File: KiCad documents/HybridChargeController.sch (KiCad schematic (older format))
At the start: 10 parts

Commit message: switched to transistors maybe need 10k
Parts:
- removed Q? (x3): 2N 7002, symbol Q_NMOS_GSD
- added Q? (x3): 2N3904, symbol Q_NPN_EBC
- added R?: 10k, symbol R
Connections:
- wire segments 28 -> 32
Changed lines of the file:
@@
-$EndComp
-$Comp
-L Q_NMOS_GSD Q?
-U 1 1 58D3AC23
-P 2950 4600
-F 0 "Q?" H 3250 4650 50  0000 R CNN
-F 1 "2N 7002" H 3450 4550 50  0000 R CNN
-F 2 "" H 3150 4700 50  0000 C CNN
-F 3 "" H 2950 4600 50  0000 C CNN
-	1    2950 4600
-	1    0    0    -1
 $EndComp
 $Comp
@@
 $EndComp
 $Comp
-L Q_NMOS_GSD Q?
-U 1 1 58D3CBFA
-P 2200 2050
-F 0 "Q?" H 2500 2100 50  0000 R CNN
-F 1 "2N 7002" H 2700 2000 50  0000 R CNN
-F 2 "" H 2400 2150 50  0000 C CNN
-F 3 "" H 2200 2050 50  0000 C CNN
-	1    2200 2050
-	1    0    0    -1
-$EndComp
-$Comp
 L Q_PMOS_GDS Q?
 U 1 1 58D3CC00
@@
 LA switch circuit \nLoad switch is closed, when SW_BAT is LOW
 $Comp
-L Q_NMOS_GSD Q?
-U 1 1 58D8C0D3
-P 1500 4750
-F 0 "Q?" H 1800 4800 50  0000 R CNN
-F 1 "2N 7002" H 2000 4700 50  0000 R CNN
-F 2 "" H 1700 4850 50  0000 C CNN
-F 3 "" H 1500 4750 50  0000 C CNN
-	1    1500 4750
-	1    0    0    -1
-$EndComp
-$Comp
 L R R?
 U 1 1 58D8C1D7
@@
 Wire Wire Line
 	1300 4750 1100 4750
+$Comp
+L Q_NPN_EBC Q?
+U 1 1 58D8E9F2
+P 1500 4750
+F 0 "Q?" H 1800 4800 50  0000 R CNN
+F 1 "2N3904" H 1950 4700 50  0000 R CNN
+F 2 "" H 1700 4850 50  0000 C CNN
+F 3 "" H 1500 4750 50  0000 C CNN
+	1    1500 4750
+	1    0    0    -1
+$EndComp
+$Comp
+L Q_NPN_EBC Q?
+U 1 1 58D8EBDE
+P 2950 4600
+F 0 "Q?" H 3250 4650 50  0000 R CNN
+F 1 "2N3904" H 3400 4550 50  0000 R CNN
+F 2 "" H 3150 4700 50  0000 C CNN
+F 3 "" H 2950 4600 50  0000 C CNN
+	1    2950 4600
+	1    0    0    -1
+$EndComp
+$Comp
+L Q_NPN_EBC Q?
+U 1 1 58D8EC57
+P 2200 2050
+F 0 "Q?" H 2500 2100 50  0000 R CNN
+F 1 "2N3904" H 2650 2000 50  0000 R CNN
+F 2 "" H 2400 2150 50  0000 C CNN
+F 3 "" H 2200 2050 50  0000 C CNN
+	1    2200 2050
+	1    0    0    -1
+$EndComp
+$Comp
+L R R?
+U 1 1 58D8EEFB
+P 3850 4400
+F 0 "R?" V 3930 4400 50  0000 C CNN
+F 1 "10k" V 3850 4400 50  0000 C CNN
+F 2 "" V 3780 4400 50  0000 C CNN
+F 3 "" H 3850 4400 50  0000 C CNN
+	1    3850 4400
+	1    0    0    -1
+$EndComp
+Wire Wire Line
+	3850 4250 3850 4000
+Connection ~ 3850 4000
+Wire Wire Line
+	3850 4550 3850 4900
+Wire Wire Line
+	3850 4900 3600 4900
+Wire Wire Line
+	3600 4900 3600 5200
+Connection ~ 3600 5200
 $EndSCHEMATC

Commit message: two mosfets on both power lines. working nicely
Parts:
- removed Q? (x2): IPD90P04P4_05, symbol Q_PMOS_GDS
- removed R?: 10k, symbol R
- added D?: D, symbol D
- added Q? (x5): IPD90P04P4_05, symbol Q_NMOS_GSD
- added Q?: 2N3904, symbol Q_NPN_EBC
- added R? (x3): 10k, symbol R
- added R?: 47k, symbol R
- added R?: 100k, symbol R
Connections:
- net labels added: COM+, LA+, LI+, LOAD+, SW_LA, SW_LI, SW_LOAD
- net labels removed: LA_12V, LA_GND, SW_BAT, VCC
- wire segments 32 -> 61
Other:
- note added: "????"
- note added: "LA switch circuit \nswitch is closed, when SW_LA is LOW"
- note added: "LI switch circuit \nswitch is open, when SW_LI is LOW"
- note added: "Load switch circuit \nswitch is open, when SW_LOAD is LOW"
- note removed: "LA switch circuit \nLoad switch is closed, when SW_BAT is LOW"
- moved on the sheet: Q?, R?

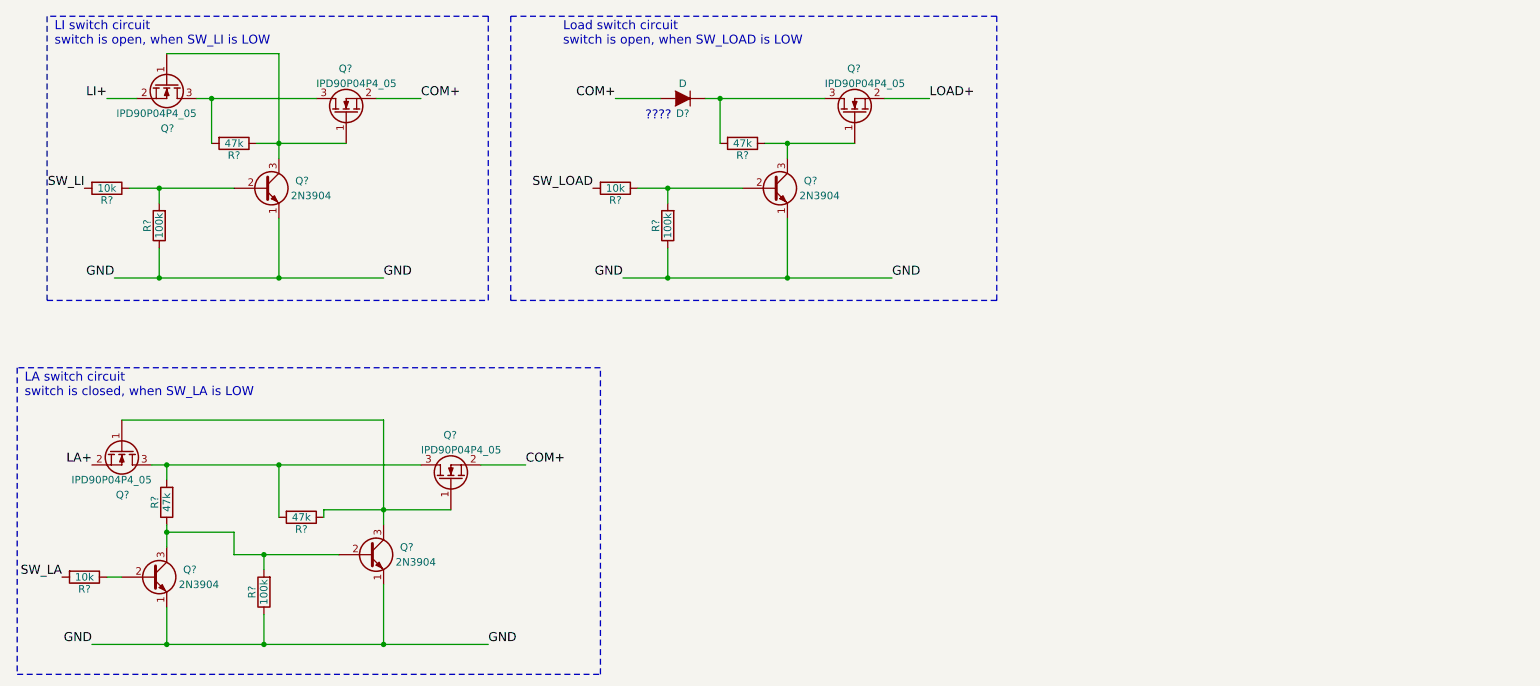
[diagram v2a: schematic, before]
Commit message: added arduinouno footprint
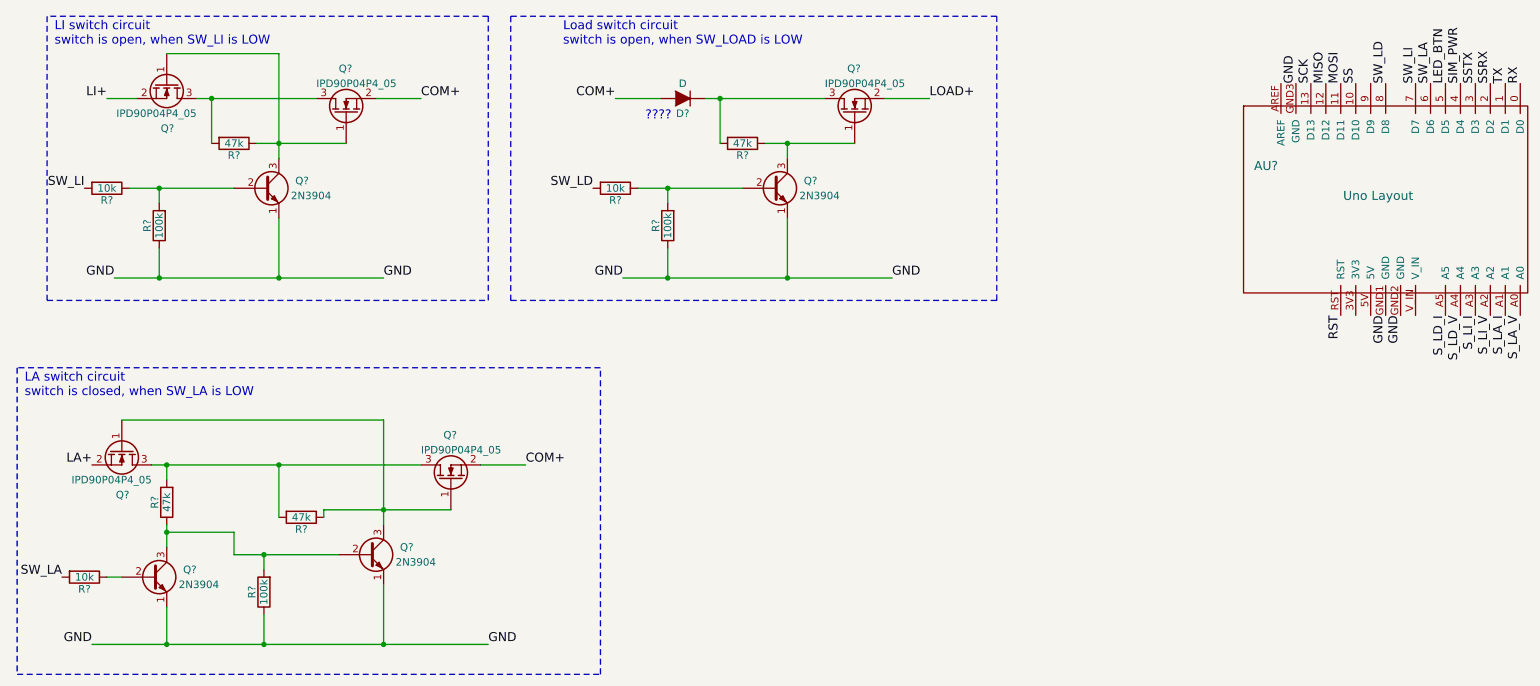
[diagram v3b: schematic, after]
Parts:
- added AU?: Uno Layout, symbol ArduinoUno
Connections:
- net GND: now also AU?.GND1 (GND), AU?.GND2 (GND), AU?.GND3 (GND)
- net SW_LA: now also AU?.6 (D6)
- net SW_LI: now also AU?.7 (D7)
- net SW_LOAD renamed SW_LD
- net SW_LD: now also AU?.8 (D8)
- new net LED_BTN: AU?.5 (D5)
- new net MISO: AU?.12 (D12)
- new net MOSI: AU?.11 (D11)
- new net RST: AU?.RST
- new net RX: AU?.0 (D0)
- new net SCK: AU?.13 (D13)
- new net SIM_PWR: AU?.4 (D4)
- new net SS: AU?.10 (D10)
- new net SSRX: AU?.2 (D2)
- new net SSTX: AU?.3 (D3)
- new net S_LA_I: AU?.A1
- new net S_LA_V: AU?.A0
- new net S_LD_I: AU?.A5
- new net S_LD_V: AU?.A4
- new net S_LI_I: AU?.A3
- new net S_LI_V: AU?.A2
- new net TX: AU?.1 (D1)
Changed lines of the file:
@@
 LIBS:contrib
 LIBS:valves
+LIBS:arduinouno
 LIBS:HybridChargeController-cache
 EELAYER 25 0
@@
 $EndComp
 Wire Wire Line
-	2600 3850 3000 3850
-Wire Wire Line
-	3000 3850 3450 3850
-Wire Wire Line
-	3000 3250 3000 3850
-Wire Wire Line
-	3000 3850 3000 3950
-Wire Wire Line
-	1050 4750 1550 4750
-Wire Wire Line
-	1550 4750 2200 4750
-Wire Wire Line
-	2200 4750 3000 4750
-Wire Wire Line
-	3000 4750 3700 4750
+	2600 3850 3450 3850
+Wire Wire Line
+	3000 3250 3000 3950
+Wire Wire Line
+	1050 4750 3700 4750
 Text Label 1050 4750 2    60   ~ 0
 GND
@@
 Connection ~ 2200 4750
 Wire Wire Line
-	2000 4150 2200 4150
-Wire Wire Line
-	2200 4150 2700 4150
+	2000 4150 2700 4150
 Wire Wire Line
 	2200 4150 2200 4250
@@
 	2300 3550 2300 3900
 Wire Wire Line
-	1450 3550 1550 3550
-Wire Wire Line
-	1550 3550 2300 3550
-Wire Wire Line
-	2300 3550 3250 3550
+	1450 3550 3250 3550
 Connection ~ 2300 3550
 Text Label 1050 3550 2    60   ~ 0
@@
 $EndComp
 Wire Wire Line
-	2150 1400 2300 1400
-Wire Wire Line
-	2300 1400 2750 1400
-Wire Wire Line
-	2300 800  2300 1400
-Wire Wire Line
-	2300 1400 2300 1500
-Wire Wire Line
-	1200 2300 1500 2300
-Wire Wire Line
-	1500 2300 2300 2300
-Wire Wire Line
-	2300 2300 3000 2300
+	2150 1400 2750 1400
+Wire Wire Line
+	2300 800  2300 1500
+Wire Wire Line
+	1200 2300 3000 2300
 Text Label 1200 2300 2    60   ~ 0
 GND
@@
 Connection ~ 1500 2300
 Wire Wire Line
-	1300 1700 1500 1700
-Wire Wire Line
-	1500 1700 2000 1700
+	1300 1700 2000 1700
 Wire Wire Line
 	1500 1700 1500 1800
@@
 	1850 1400 1850 1100
 Wire Wire Line
-	1750 1100 1850 1100
-Wire Wire Line
-	1850 1100 2550 1100
+	1750 1100 2550 1100
 Connection ~ 1850 1100
 Text Label 1150 1100 2    60   ~ 0
@@
 Connection ~ 1550 3550
 Wire Wire Line
-	1550 3950 1550 4000
-Wire Wire Line
-	1550 4000 1550 4100
+	1550 3950 1550 4100
 Wire Wire Line
 	1550 4000 2000 4000
@@
 $EndComp
 Wire Wire Line
-	5550 1400 5700 1400
-Wire Wire Line
-	5700 1400 6150 1400
-Wire Wire Line
-	4600 2300 4900 2300
-Wire Wire Line
-	4900 2300 5700 2300
-Wire Wire Line
-	5700 2300 6400 2300
+	5550 1400 6150 1400
+Wire Wire Line
+	4600 2300 6400 2300
 Text Label 4600 2300 2    60   ~ 0
 GND
@@
 Connection ~ 4900 2300
 Wire Wire Line
-	4700 1700 4900 1700
-Wire Wire Line
-	4900 1700 5400 1700
+	4700 1700 5400 1700
 Wire Wire Line
 	4900 1700 4900 1800
 Connection ~ 4900 1700
 Text Label 4400 1700 2    60   ~ 0
-SW_LOAD
+SW_LD
 Wire Wire Line
 	6350 1100 6650 1100
@@
 	5250 1400 5250 1100
 Wire Wire Line
-	5150 1100 5250 1100
-Wire Wire Line
-	5250 1100 5950 1100
+	5150 1100 5950 1100
 Connection ~ 5250 1100
 Text Label 6650 1100 0    60   ~ 0
@@
 Text Notes 4750 1250 0    60   ~ 0
 ????
+$Comp
+L ArduinoUno AU?
+U 1 1 58EE210F
+P 8200 1700
+F 0 "AU?" H 8900 1850 60  0000 C CNN
+F 1 "Uno Layout" H 9650 1650 60  0000 C CNN
+F 2 "" H 8200 1700 60  0001 C CNN
+F 3 "" H 8200 1700 60  0001 C CNN
+	1    8200 1700
+	1    0    0    -1
+$EndComp
+Text Label 9100 1000 1    60   ~ 0
+GND
+Text Label 9700 2550 3    60   ~ 0
+GND
+Text Label 9800 2550 3    60   ~ 0
+GND
+Text Label 10600 1000 1    60   ~ 0
+RX
+Text Label 10500 1000 1    60   ~ 0
+TX
+Text Label 10400 1000 1    60   ~ 0
+SSRX
+Text Label 10300 1000 1    60   ~ 0
+SSTX
+Text Label 10200 1000 1    60   ~ 0
+SIM_PWR
+Text Label 10100 1000 1    60   ~ 0
+LED_BTN
+Text Label 9500 1000 1    60   ~ 0
+SS
+Text Label 9400 1000 1    60   ~ 0
+MOSI
+Text Label 9300 1000 1    60   ~ 0
+MISO
+Text Label 9200 1000 1    60   ~ 0
+SCK
+Text Label 10000 1000 1    60   ~ 0
+SW_LA
+Text Label 9900 1000 1    60   ~ 0
+SW_LI
+Text Label 9700 1000 1    60   ~ 0
+SW_LD
+Text Label 9400 2550 3    60   ~ 0
+RST
+Text Label 10600 2550 3    60   ~ 0
+S_LA_V
+Text Label 10500 2550 3    60   ~ 0
+S_LA_I
+Text Label 10400 2550 3    60   ~ 0
+S_LI_V
+Text Label 10300 2550 3    60   ~ 0
+S_LI_I
+Text Label 10200 2550 3    60   ~ 0
+S_LD_V
+Text Label 10100 2550 3    60   ~ 0
+S_LD_I
 $EndSCHEMATC

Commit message: added two sensor circuits
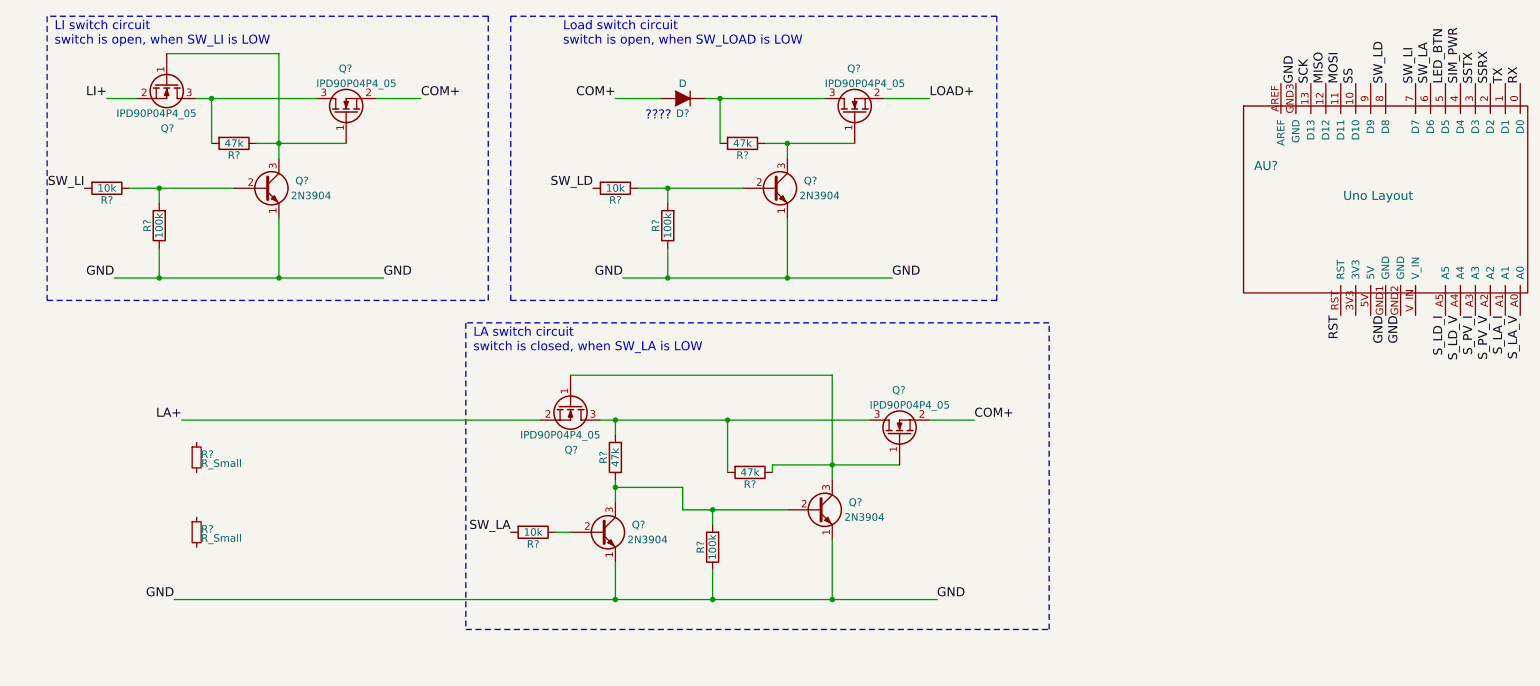
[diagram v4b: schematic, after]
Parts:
- added R? (x2): R_Small, symbol R_Small
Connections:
- net S_LI_I renamed S_PV_I
- net S_LI_V renamed S_PV_V
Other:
- moved on the sheet: Q?, R?
